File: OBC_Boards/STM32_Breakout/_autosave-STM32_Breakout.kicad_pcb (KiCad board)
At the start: 4 copper layers, 95 x 95 mm, 96 parts, among them J1 Conn_02x20_Odd_Even, J2 ST1W008S4ER1500-MicroSDConnec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, J3 1050171001, J4 105017-1001, J5 1050171001, J6 SSQ-105-03-T-D, J7 SSQ-105-03-T-D, Q1 Q_PMOS_DGS, U1 MR25H10MDF, U2 BU33SA5WGWZ-E2-qsat-symb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

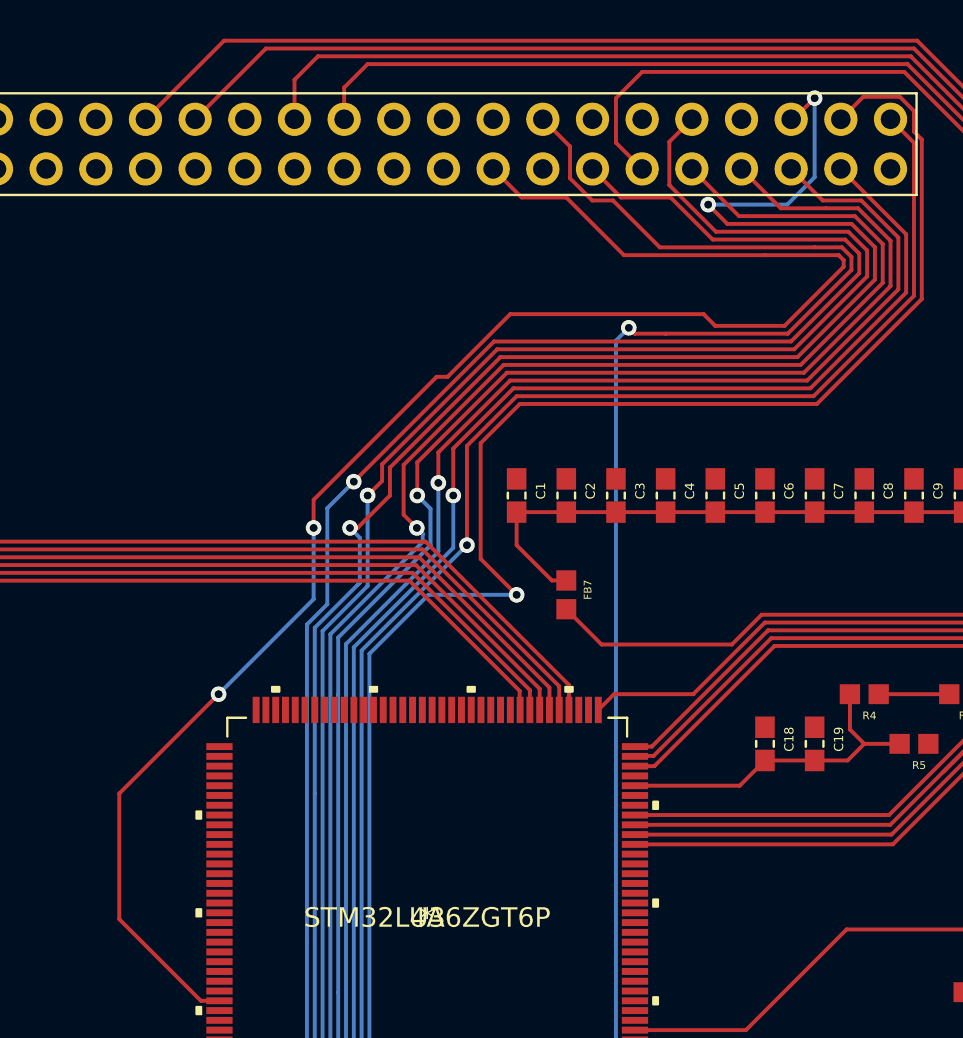
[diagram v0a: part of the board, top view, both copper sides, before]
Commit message: Started tracing
Added traces with J7 and J6 connectors to STM32. Connected power circuit.
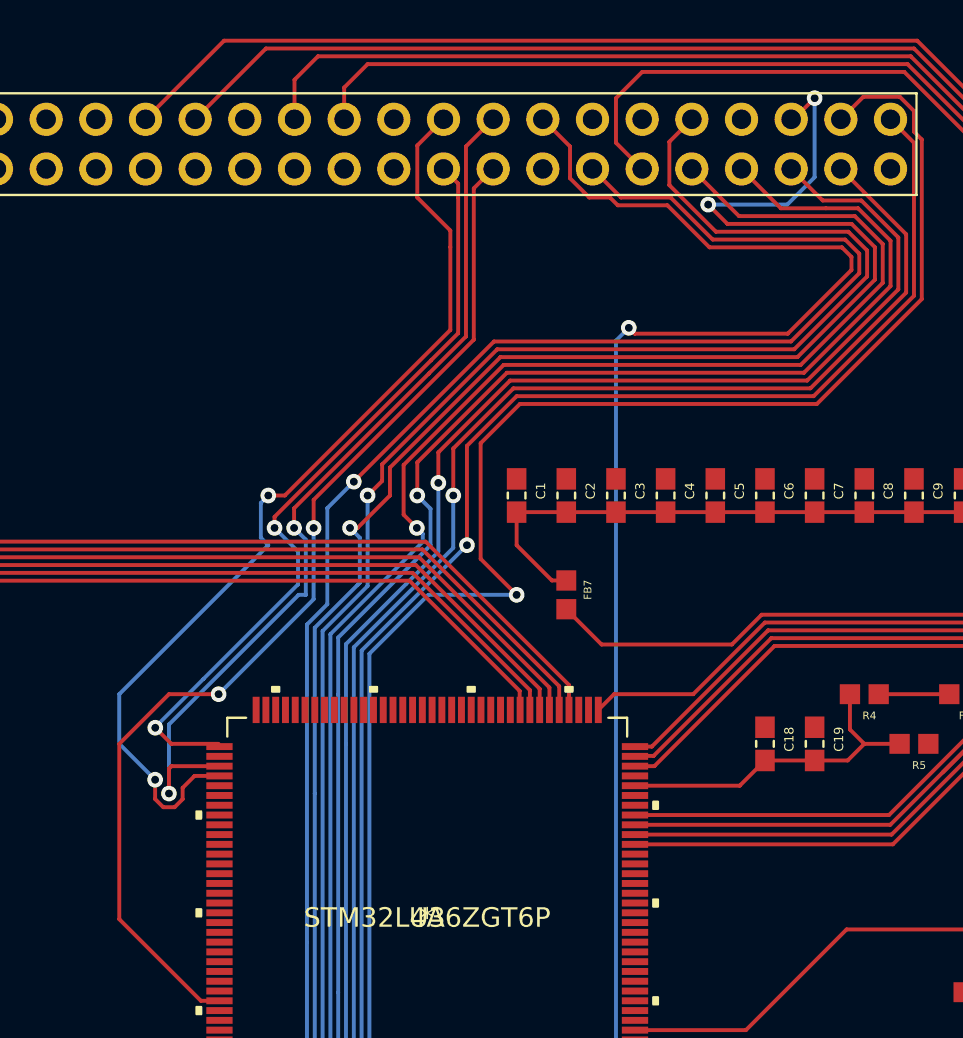
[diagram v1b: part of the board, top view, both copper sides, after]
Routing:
- net SPI2_MOSI: track 0.00 -> 49.1 mm, vias 0 -> 2
- net SPI2_MISO: track 0.00 -> 46.0 mm, vias 0 -> 2
- net GPIO7: track 0.00 -> 39.9 mm, vias 0 -> 2
- net GPIO8: track 85.1 -> 54.6 mm
